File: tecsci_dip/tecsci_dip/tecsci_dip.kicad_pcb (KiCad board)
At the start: 2 copper layers, 65 x 60 mm, 41 parts, among them IC201 TMC5130, J201 Conn_01x19_ESP32, J202 Conn_01x19_ESP32, U201 AKL182_04_POL_HEADER, U301 Regulador_LM5161

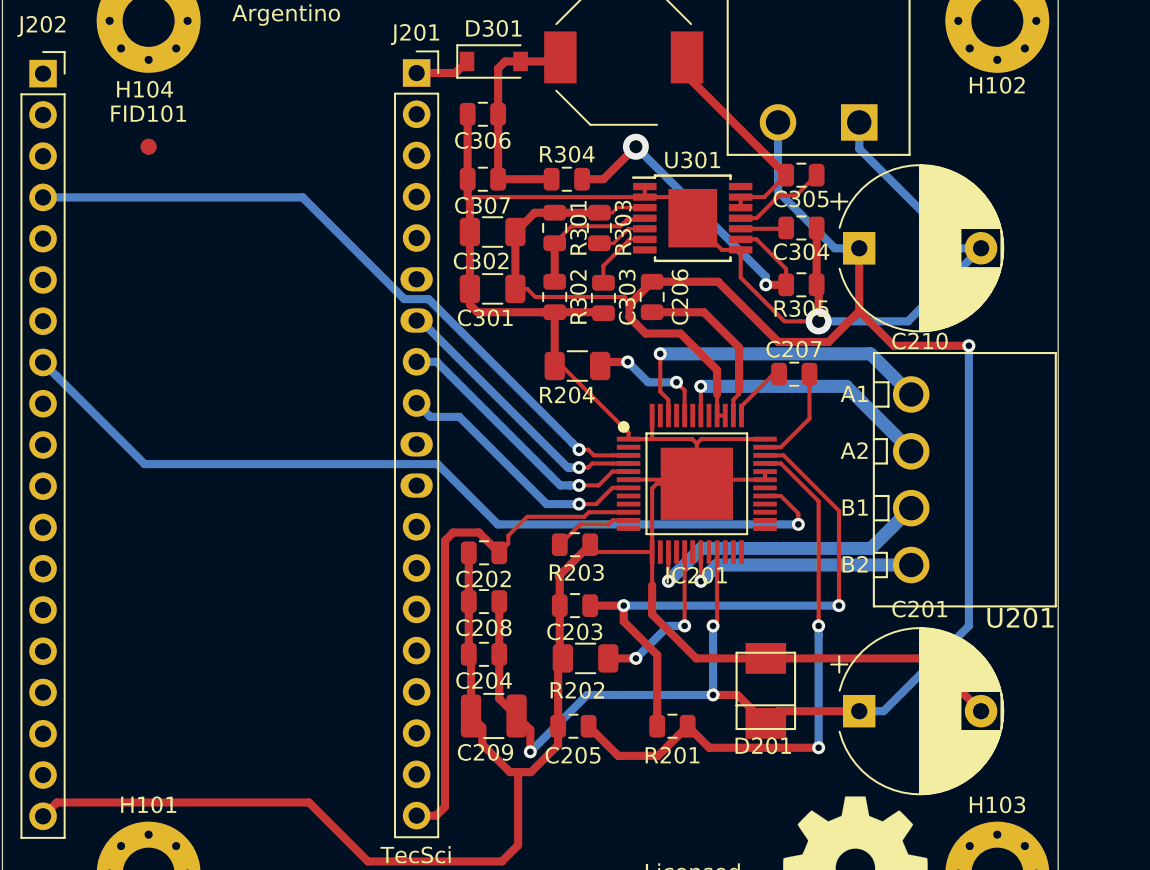
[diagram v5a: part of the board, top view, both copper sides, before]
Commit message: arreglo en alimentacion.sch , habria con error en archivo
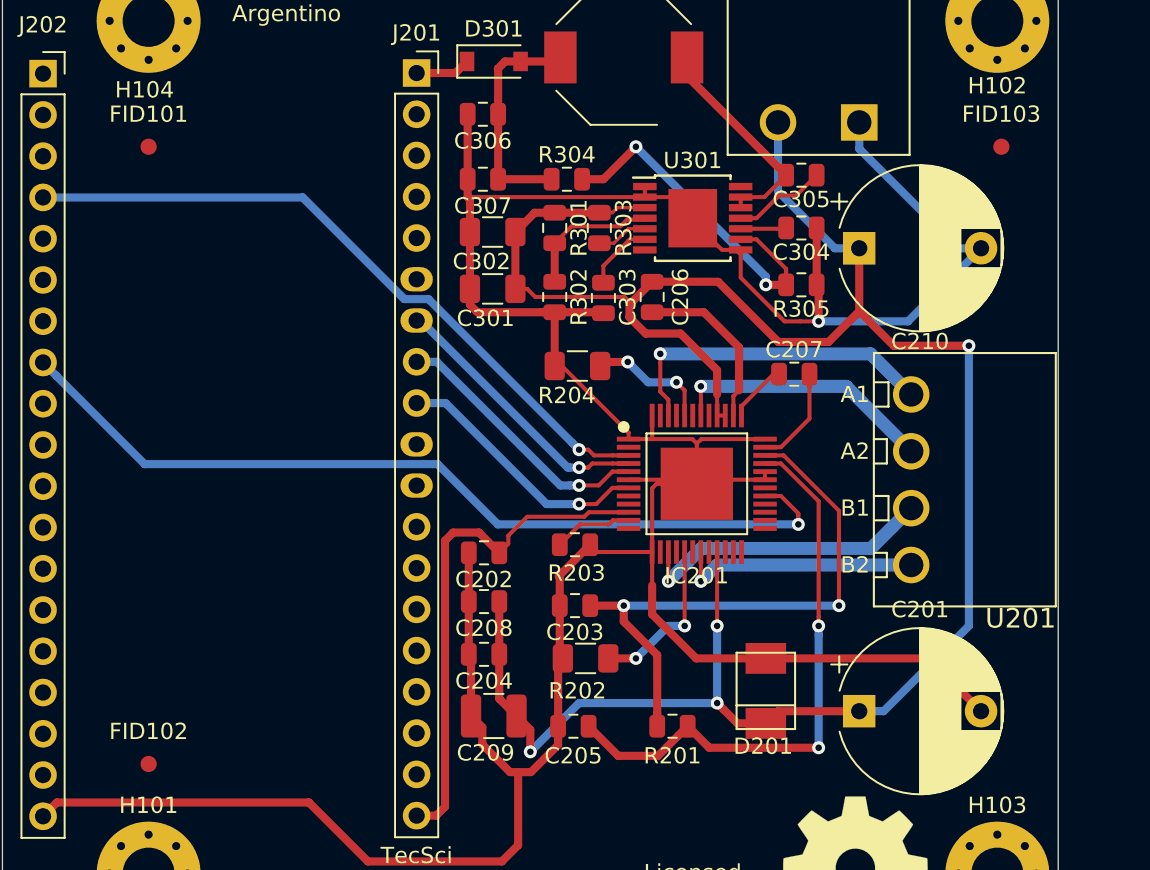
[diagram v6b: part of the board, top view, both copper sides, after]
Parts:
- added FID102: Fiducial, Fiducial:Fiducial_1mm_Mask2mm, F.Cu at (65.0, 104.5)
- added FID103: Fiducial, Fiducial:Fiducial_1mm_Mask2mm, F.Cu at (117.5, 66.5)
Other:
- board text added: "Grilla de posicionamiento: Principal 0,25mm Grilla de ruteo: Principal 0,25mm Mounting Hole: Principal: 3,2mm Pistas: Principal 0.5mm Alternativa inferior 0.25mm (Límite Mayer 8mils - 0.20mm) Alternativa superior 0,8mm Vías: Principal 0.8mm/0.4mm (Límite Mayer 8mils - 0.80mm) Margen General : 0,22 mm Margen Particular: 0,2 mm Componentes -> 201 301 (Límite Mayer 8mils - 0.18mm) Base para las rest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"
- board text removed: "Grilla de posicionamiento: Principal 0,25mm Grilla de ruteo: Principal 0,25mm Mounting Hole: Principal: 3,2mm Pistas: Principal 0.5mm Alternativa inferior 0.25mm (Límite Mayer 8mils - 0.20mm) Alternativa superior 0,8mm Vías: Principal 1.6mm/0.8mm Alternativa 0.8mm/0.4mm (Límite Mayer 8mils - 0.80mm) Margen General : 0,22 mm Margen Particular: 0,2 mm Componentes -> 201 301 (Límite Mayer 8mils - 0.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"
